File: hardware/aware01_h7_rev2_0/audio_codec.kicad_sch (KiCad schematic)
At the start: 10 parts, among them IC1 TLV320AIC3204IRHBR

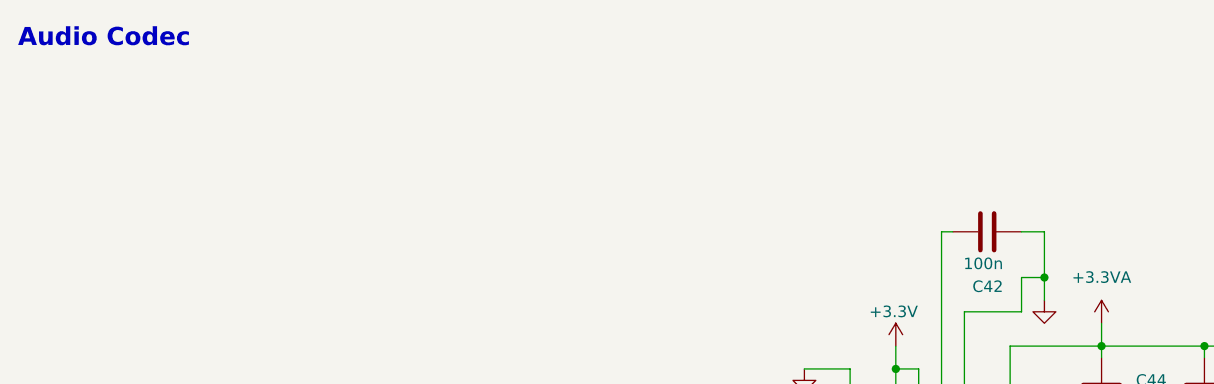
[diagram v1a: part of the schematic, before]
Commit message: schematic formatting
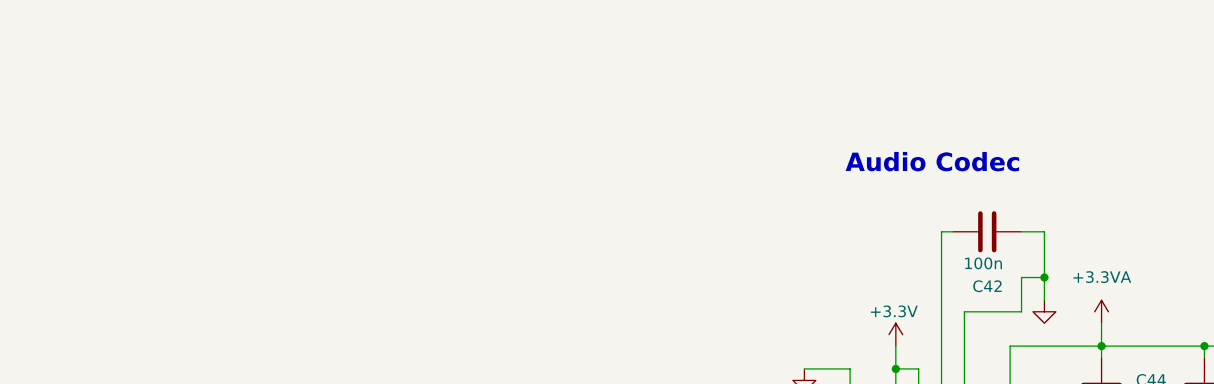
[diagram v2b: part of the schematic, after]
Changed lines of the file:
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@@
 	(text "Audio Codec"
 		(exclude_from_sim no)
-		(at 16.764 16.764 0)
+		(at 108.712 30.734 0)
 		(effects
 			(font
-				(size 2 2)
+				(size 2.032 2.032)
 				(thickness 0.4)
 				(bold yes)

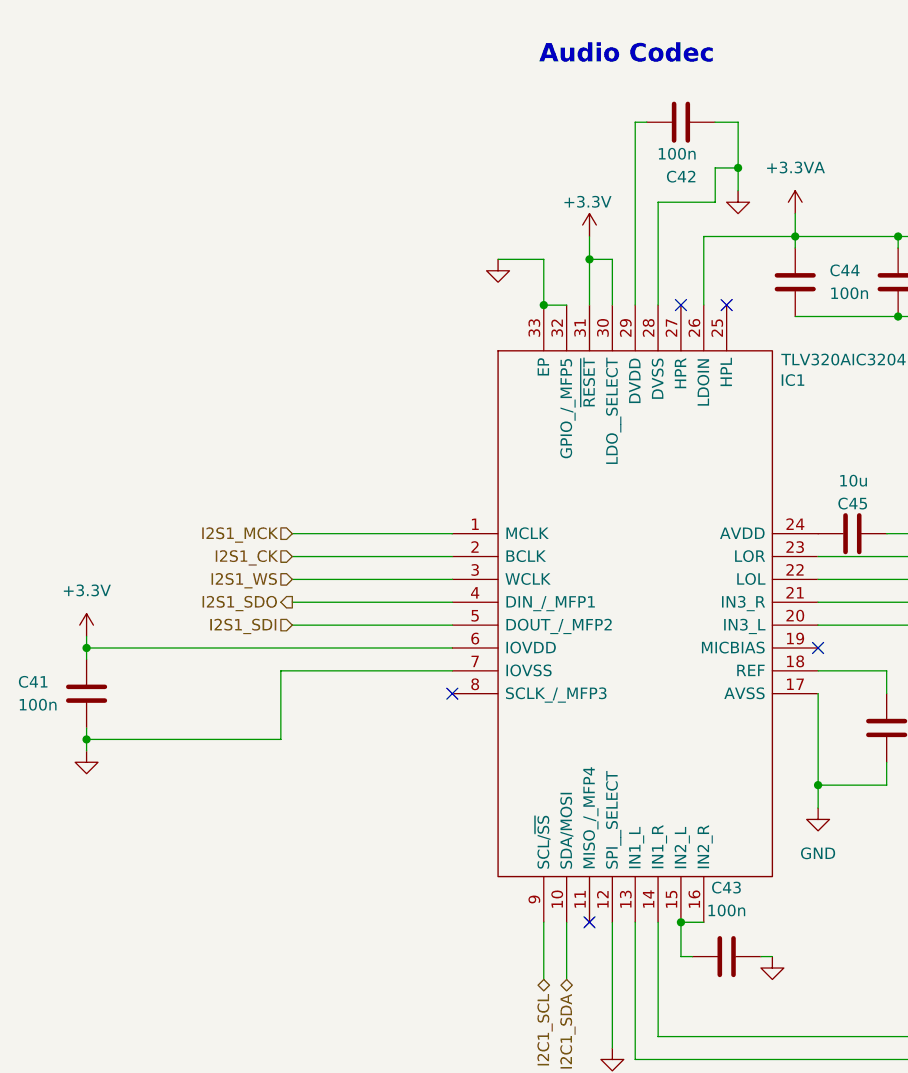
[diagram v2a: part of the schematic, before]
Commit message: refine layout, add testpoints
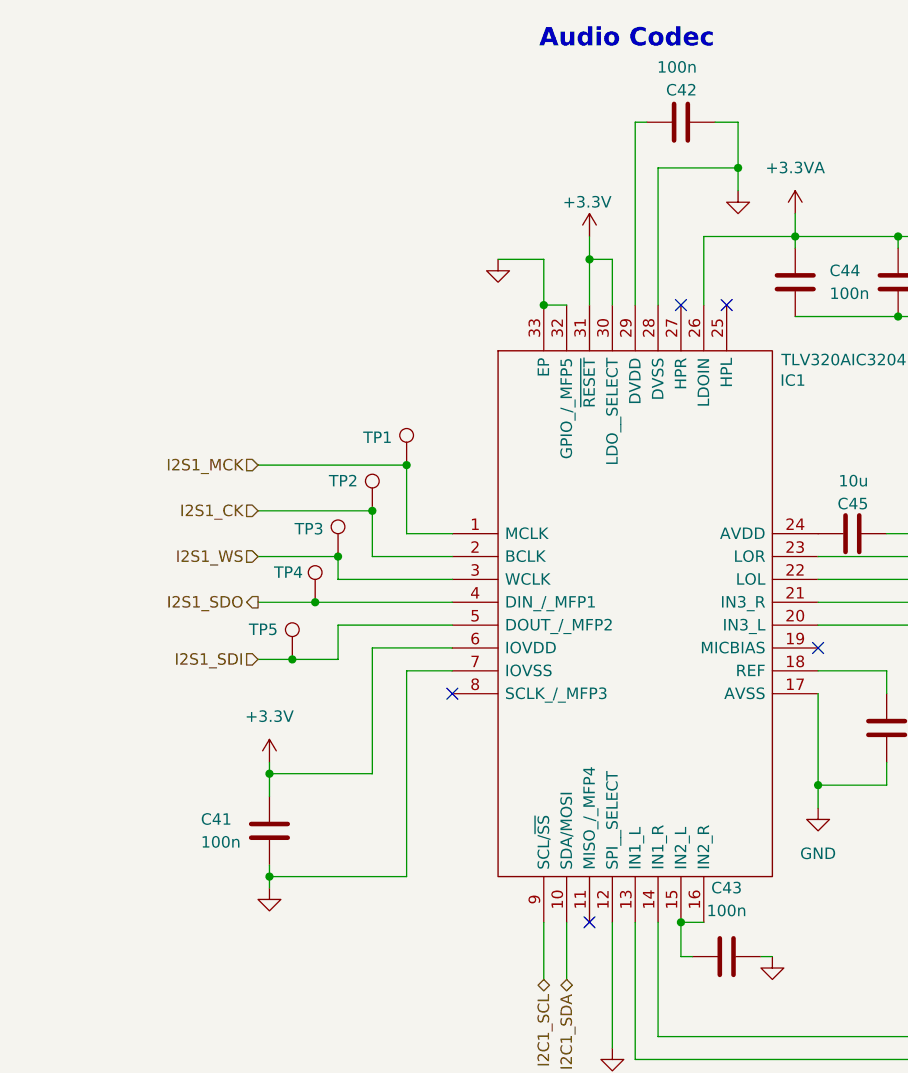
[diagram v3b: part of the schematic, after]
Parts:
- added TP1, TP2, TP3, TP4, TP5: TestPoint, TestPoint:TestPoint_Pad_D1.0mm, symbol Connector:TestPoint
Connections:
- net I2S1_CK: now also TP2.1
- net I2S1_MCK: now also TP1.1
- net I2S1_SDI: now also TP5.1
- net I2S1_SDO: now also TP4.1
- net I2S1_WS: now also TP3.1
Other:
- moved on the sheet: C41

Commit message: hardware: update analog sim and routing (wip)
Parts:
- renumbered C41 to C37, C42 to C38, C43 to C39, C44 to C40, C45 to C41, C46 to C42, C8 to C43, C9 to C44, C47 to C45, IC1 to IC5, TP5 to TP1, TP4 to TP2, TP2 to TP4, TP1 to TP5
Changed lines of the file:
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@@
 		(on_board yes)
 		(dnp no)
-		(property "Reference" "#PWR067"
+		(property "Reference" "#PWR080"
 			(at 167.64 91.44 0)
 			(effects
@@
 			(project "ima_new_codec"
 				(path "/efd43d7c-3c18-45dd-8fa5-4bf32165850f/50dd69da-5058-483c-924f-252f04b072bd"
-					(reference "#PWR067")
+					(reference "#PWR080")
 					(unit 1)
 				)
@@
 		(dnp no)
 		(fields_autoplaced yes)
-		(property "Reference" "#PWR064"
+		(property "Reference" "#PWR078"
 			(at 160.02 68.58 0)
 			(effects
@@
 			(project "aware01_h7"
 				(path "/efd43d7c-3c18-45dd-8fa5-4bf32165850f/50dd69da-5058-483c-924f-252f04b072bd"
-					(reference "#PWR064")
+					(reference "#PWR078")
 					(unit 1)
 				)
@@
 		(on_board yes)
 		(dnp no)
-		(property "Reference" "C9"
+		(property "Reference" "C44"
 			(at 163.83 55.8799 0)
 			(effects
@@
 			(project "aware01_h7_rev1_3"
 				(path "/efd43d7c-3c18-45dd-8fa5-4bf32165850f/50dd69da-5058-483c-924f-252f04b072bd"
-					(reference "C9")
+					(reference "C44")
 					(unit 1)
 				)
@@
 		(on_board yes)
 		(dnp no)
-		(property "Reference" "#PWR059"
+		(property "Reference" "#PWR072"
 			(at 114.3 55.88 0)
 			(effects
@@
 			(project "ima_new_codec"
 				(path "/efd43d7c-3c18-45dd-8fa5-4bf32165850f/50dd69da-5058-483c-924f-252f04b072bd"
-					(reference "#PWR059")
+					(reference "#PWR072")
 					(unit 1)
 				)
@@
 		(dnp no)
 		(fields_autoplaced yes)
-		(property "Reference" "#PWR062"
+		(property "Reference" "#PWR075"
 			(at 134.62 138.43 0)
 			(effects
@@
 			(project "ima_new_codec"
 				(path "/efd43d7c-3c18-45dd-8fa5-4bf32165850f/50dd69da-5058-483c-924f-252f04b072bd"
-					(reference "#PWR062")
+					(reference "#PWR075")
 					(unit 1)
 				)
@@
 		(on_board yes)
 		(dnp no)
-		(property "Reference" "C46"
+		(property "Reference" "C42"
 			(at 150.114 106.68 0)
 			(effects
@@
 			(project "ima_new_codec"
 				(path "/efd43d7c-3c18-45dd-8fa5-4bf32165850f/50dd69da-5058-483c-924f-252f04b072bd"
-					(reference "C46")
+					(reference "C42")
 					(unit 1)
 				)
@@
 		(on_board yes)
 		(dnp no)
-		(property "Reference" "C42"
+		(property "Reference" "C38"
 			(at 126.238 35.814 90)
 			(effects
@@
 			(project "ima_new_codec"
 				(path "/efd43d7c-3c18-45dd-8fa5-4bf32165850f/50dd69da-5058-483c-924f-252f04b072bd"
-					(reference "C42")
+					(reference "C38")
 					(unit 1)
 				)
@@
 		(on_board yes)
 		(dnp no)
-		(property "Reference" "C45"
+		(property "Reference" "C41"
 			(at 145.288 81.788 90)
 			(effects
@@
 			(project "ima_new_codec"
 				(path "/efd43d7c-3c18-45dd-8fa5-4bf32165850f/50dd69da-5058-483c-924f-252f04b072bd"
-					(reference "C45")
+					(reference "C41")
 					(unit 1)
 				)
@@
 		(on_board yes)
 		(dnp no)
-		(property "Reference" "C41"
+		(property "Reference" "C37"
 			(at 71.12 116.84 0)
 			(effects
@@
 			(project "aware01_h7_rev1_2"
 				(path "/efd43d7c-3c18-45dd-8fa5-4bf32165850f/50dd69da-5058-483c-924f-252f04b072bd"
-					(reference "C41")
+					(reference "C37")
 					(unit 1)
 				)
@@
 		(dnp no)
 		(fields_autoplaced yes)
-		(property "Reference" "#PWR066"
+		(property "Reference" "#PWR079"
 			(at 162.56 109.22 0)
 			(effects
@@
 			(project "ima_new_codec"
 				(path "/efd43d7c-3c18-45dd-8fa5-4bf32165850f/50dd69da-5058-483c-924f-252f04b072bd"
-					(reference "#PWR066")
+					(reference "#PWR079")
 					(unit 1)
 				)
@@
 		(on_board yes)
 		(dnp no)
-		(property "Reference" "IC1"
+		(property "Reference" "IC5"
 			(at 136.906 68.072 0)
 			(effects
@@
 			(project ""
 				(path "/efd43d7c-3c18-45dd-8fa5-4bf32165850f/50dd69da-5058-483c-924f-252f04b072bd"
-					(reference "IC1")
+					(reference "IC5")
 					(unit 1)
 				)
@@
 		(dnp no)
 		(fields_autoplaced yes)
-		(property "Reference" "C47"
+		(property "Reference" "C45"
 			(at 166.37 97.7899 0)
 			(effects
@@
 			(project "ima_new_codec"
 				(path "/efd43d7c-3c18-45dd-8fa5-4bf32165850f/50dd69da-5058-483c-924f-252f04b072bd"
-					(reference "C47")
+					(reference "C45")
 					(unit 1)
 				)
@@
 		(dnp no)
 		(fields_autoplaced yes)
-		(property "Reference" "#PWR056"
+		(property "Reference" "#PWR069"
 			(at 78.74 114.3 0)
 			(effects
@@
 			(project "ima_new_codec"
 				(path "/efd43d7c-3c18-45dd-8fa5-4bf32165850f/50dd69da-5058-483c-924f-252f04b072bd"
-					(reference "#PWR056")
+					(reference "#PWR069")
 					(unit 1)
 				)
@@
 		(dnp no)
 		(fields_autoplaced yes)
-		(property "Reference" "#PWR058"
+		(property "Reference" "#PWR071"
 			(at 104.14 60.96 0)
 			(effects
@@
 			(project "aware01_h7"
 				(path "/efd43d7c-3c18-45dd-8fa5-4bf32165850f/50dd69da-5058-483c-924f-252f04b072bd"
-					(reference "#PWR058")
+					(reference "#PWR071")
 					(unit 1)
 				)
@@
 		(dnp no)
 		(fields_autoplaced yes)
-		(property "Reference" "#PWR061"
+		(property "Reference" "#PWR074"
 			(at 130.81 53.34 0)
 			(effects
@@
 			(project "ima_new_codec"
 				(path "/efd43d7c-3c18-45dd-8fa5-4bf32165850f/50dd69da-5058-483c-924f-252f04b072bd"
-					(reference "#PWR061")
+					(reference "#PWR074")
 					(unit 1)
 				)
@@
 		(on_board yes)
 		(dnp no)
-		(property "Reference" "TP4"
+		(property "Reference" "TP2"
 			(at 79.248 89.408 0)
 			(effects
@@
 			(project "aware01_h7_rev2_0"
 				(path "/efd43d7c-3c18-45dd-8fa5-4bf32165850f/50dd69da-5058-483c-924f-252f04b072bd"
-					(reference "TP4")
+					(reference "TP2")
 					(unit 1)
 				)
@@
 		(dnp no)
 		(fields_autoplaced yes)
-		(property "Reference" "#PWR057"
+		(property "Reference" "#PWR070"
 			(at 78.74 130.81 0)
 			(effects
@@
 			(project "ima_new_codec"
 				(path "/efd43d7c-3c18-45dd-8fa5-4bf32165850f/50dd69da-5058-483c-924f-252f04b072bd"
-					(reference "#PWR057")
+					(reference "#PWR070")
 					(unit 1)
 				)
@@
 		(dnp no)
 		(fields_autoplaced yes)
-		(property "Reference" "C43"
+		(property "Reference" "C39"
 			(at 129.54 124.46 90)
 			(effects
@@
 			(project "ima_new_codec"
 				(path "/efd43d7c-3c18-45dd-8fa5-4bf32165850f/50dd69da-5058-483c-924f-252f04b072bd"
-					(reference "C43")
+					(reference "C39")
 					(unit 1)
 				)
@@
 		(dnp no)
 		(fields_autoplaced yes)
-		(property "Reference" "#PWR065"
+		(property "Reference" "#PWR077"
 			(at 139.7 121.92 0)
 			(effects
@@
 			(project "ima_new_codec"
 				(path "/efd43d7c-3c18-45dd-8fa5-4bf32165850f/50dd69da-5058-483c-924f-252f04b072bd"
-					(reference "#PWR065")
+					(reference "#PWR077")
 					(unit 1)
 				)
@@
 		(on_board yes)
 		(dnp no)
-		(property "Reference" "TP2"
+		(property "Reference" "TP4"
 			(at 85.344 79.248 0)
 			(effects
@@
 			(project "aware01_h7_rev2_0"
 				(path "/efd43d7c-3c18-45dd-8fa5-4bf32165850f/50dd69da-5058-483c-924f-252f04b072bd"
-					(reference "TP2")
+					(reference "TP4")
 					(unit 1)
 				)
@@
 		(on_board yes)
 		(dnp no)
-		(property "Reference" "TP5"
+		(property "Reference" "TP1"
 			(at 76.454 95.758 0)
 			(effects
@@
 			(project "aware01_h7_rev2_0"
 				(path "/efd43d7c-3c18-45dd-8fa5-4bf32165850f/50dd69da-5058-483c-924f-252f04b072bd"
-					(reference "TP5")
+					(reference "TP1")
 					(unit 1)
 				)
@@
 		(on_board yes)
 		(dnp no)
-		(property "Reference" "C8"
+		(property "Reference" "C43"
 			(at 152.4 55.8799 0)
 			(effects
@@
 			(project "aware01_h7_rev1_3"
 				(path "/efd43d7c-3c18-45dd-8fa5-4bf32165850f/50dd69da-5058-483c-924f-252f04b072bd"
-					(reference "C8")
+					(reference "C43")
 					(unit 1)
 				)
@@
 		(dnp no)
 		(fields_autoplaced yes)
-		(property "Reference" "#PWR063"
+		(property "Reference" "#PWR076"
 			(at 137.16 53.34 0)
 			(effects
@@
 			(project "ima_new_codec"
 				(path "/efd43d7c-3c18-45dd-8fa5-4bf32165850f/50dd69da-5058-483c-924f-252f04b072bd"
-					(reference "#PWR063")
+					(reference "#PWR076")
 					(unit 1)
 				)
@@
 		(on_board yes)
 		(dnp no)
-		(property "Reference" "TP1"
+		(property "Reference" "TP5"
 			(at 89.154 74.422 0)
 			(effects
@@
 			(project ""
 				(path "/efd43d7c-3c18-45dd-8fa5-4bf32165850f/50dd69da-5058-483c-924f-252f04b072bd"
-					(reference "TP1")
+					(reference "TP5")
 					(unit 1)
 				)
@@
 		(dnp no)
 		(fields_autoplaced yes)
-		(property "Reference" "#PWR060"
+		(property "Reference" "#PWR073"
 			(at 116.84 148.59 0)
 			(effects
@@
 			(project "ima_new_codec"
 				(path "/efd43d7c-3c18-45dd-8fa5-4bf32165850f/50dd69da-5058-483c-924f-252f04b072bd"
-					(reference "#PWR060")
+					(reference "#PWR073")
 					(unit 1)
 				)
@@
 		(on_board yes)
 		(dnp no)
-		(property "Reference" "C44"
+		(property "Reference" "C40"
 			(at 140.97 55.8799 0)
 			(effects
@@
 			(project ""
 				(path "/efd43d7c-3c18-45dd-8fa5-4bf32165850f/50dd69da-5058-483c-924f-252f04b072bd"
-					(reference "C44")
-					(unit 1)
-				)
+					(reference "C40")
+					(unit 1)
+				)

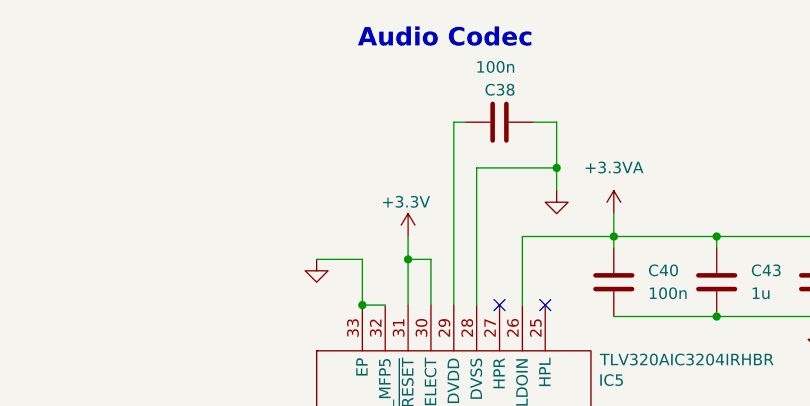
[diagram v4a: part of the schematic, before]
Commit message: hardware: update layout
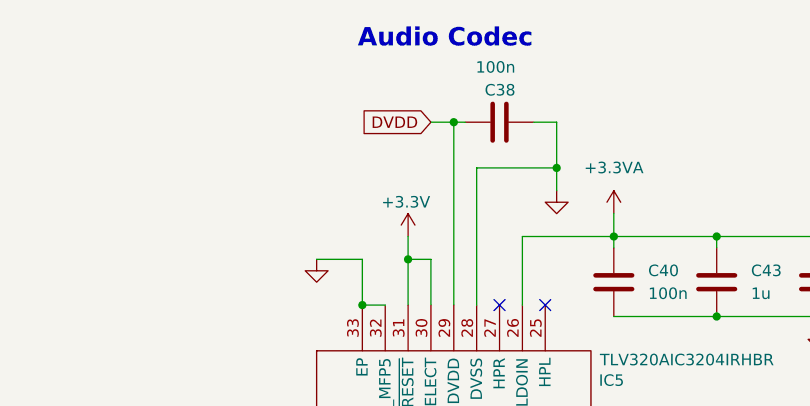
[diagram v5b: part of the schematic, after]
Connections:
- net DVDD: now reaches C38.2, IC5.29 (DVDD)
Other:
- company: (none) -> Ausschussware
- title: (none) -> Aware 01 - Eurorack DSP Module
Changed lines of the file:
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@@
 	(generator_version "9.0")
 	(paper "A4")
+	(title_block
+		(title "Aware 01 - Eurorack DSP Module")
+		(date "2025-12-19")
+		(rev "2")
+		(company "Ausschussware")
+		(comment 1 "Jonas Bengt Lux")
+		(comment 2 "TH Köln")
+		(comment 3 "Bachelor Technische Informatik")
+	)
 	(text "Audio Codec"
 		(exclude_from_sim no)
@@
 	)
 	(junction
+		(at 119.38 39.37)
+		(diameter 0)
+		(color 0 0 0 0)
+	)
+	(junction
 		(at 78.74 111.76)
 		(diameter 0)
@@
 	(wire
 		(pts
+			(xy 119.38 39.37) (xy 119.38 59.69)
+		)
+		(stroke
+			(width 0)
+			(type default)
+		)
+	)
+	(wire
+		(pts
 			(xy 119.38 39.37) (xy 120.65 39.37)
 		)
@@
 	(wire
 		(pts
-			(xy 119.38 39.37) (xy 119.38 59.69)
-		)
-		(stroke
-			(width 0)
-			(type default)
-		)
-	)
-	(wire
-		(pts
 			(xy 109.22 59.69) (xy 109.22 54.61)
 		)
@@
 	(wire
 		(pts
+			(xy 116.84 39.37) (xy 119.38 39.37)
+		)
+		(stroke
+			(width 0)
+			(type default)
+		)
+	)
+	(wire
+		(pts
 			(xy 148.59 52.07) (xy 148.59 53.34)
 		)
@@
 		)
 	)
+	(global_label "DVDD"
+		(shape input)
+		(at 116.84 39.37 180)
+		(fields_autoplaced yes)
+		(effects
+			(font
+				(size 1.27 1.27)
+			)
+			(justify right)
+		)
+		(property "Intersheetrefs" "${INTERSHEET_REFS}"
+			(at 108.9562 39.37 0)
+			(effects
+				(font
+					(size 1.27 1.27)
+				)
+				(justify right)
+				(hide yes)
+			)
+		)
+	)
